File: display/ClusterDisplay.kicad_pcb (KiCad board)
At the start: 4 copper layers, 169.3 x 101.8 mm, 164 parts, among them J1 Verdin iMX95 Hexa 8GB WB IT, J10 RTC coin cell, J11 Molex KK-254 22-27-2041, rota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, J12 Samtec TSW-103-07-G-S A55 con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, J13 Samtec TSW-105-07-G-S USB_1 O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, J14 JST XH B5B-XH-A balanced line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, J15 JST XH B3B-XH-A electret micr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, J16 MFi coprocessor access I2C_1 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, J17 GCT USB4105-GF-A USB-C 2.0 ho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, J2 Phoenix MKDS 1,5/3-5,08 power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, J3 Molex KK-254 22-27-2031 priva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, J4 TST040HDBC-42 panel, J8 Samtec TSW-108-07-G-S JTAG (b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, J9 Samtec TSW-104-07-G-S buttons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, Q1 PMV55ENEA (AEC-Q101, 60V/20V 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, Q2 PMV55ENEA (AEC-Q101, 60V/20V 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, Q3 PMV55ENEA ignition wake pulld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, U1 LM74930-Q1, U10 TLV767-Q1 (3.3 V audio AVDD), U11 TPS2557-Q1, U12 TPD4E05U06-Q1 line-out ESD, U13 TPD4E05U06-Q1 mic ESD, U14 TPD4E05U06-Q1 USB ESD, U2 LM61460-Q1, U3 TLV767-Q1, U4 TCAN1044V-Q1, U6 TPS65131-Q1, U7 TPS61165-Q1, U8 TPS22918-Q1 (AEC-Q100 G2) dia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, U9 TAC5112-Q1

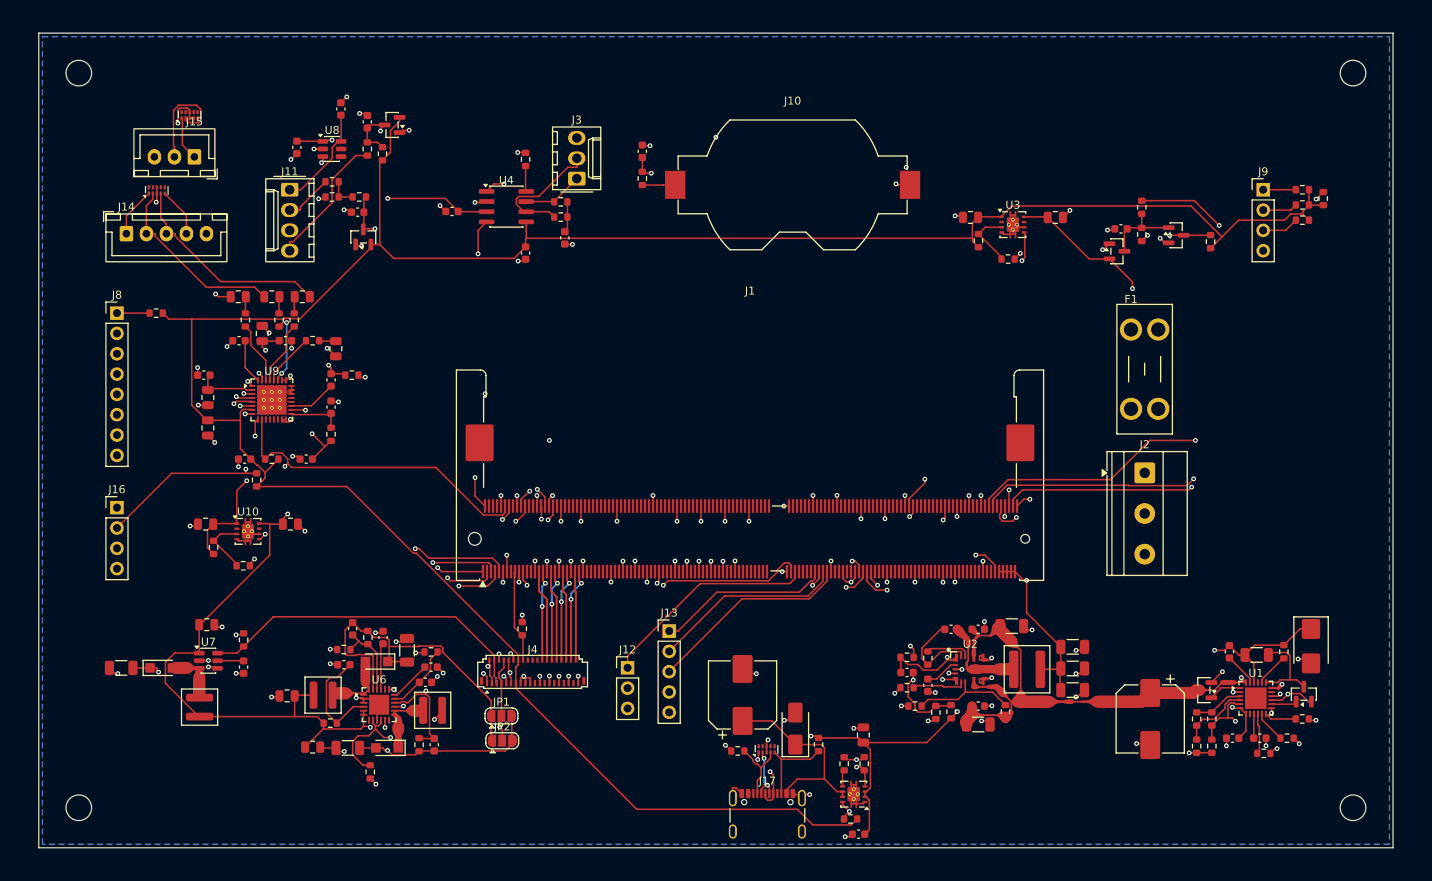
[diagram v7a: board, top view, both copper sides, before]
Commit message: Electrical review, part 2: +3V3 rail clamp on gauges, display battery path and TVS footprint, harness wording, new display parts reviewed
gauges/: D33 (onsemi SZMMSZ3V6T1G 3.6 V zener) clamps +3V3 when a sender wire is shorted to battery with the car off (G-08); BOM and connector values follow docs/harness.md (J7 DTM06-6S with a sealed cavity, J8 an in-dash KK 254 cable, 20/22 AWG). display/: D1 footprint D_SMB -> D_SMC to match the SMCJ33A in the BOM (D-01); VBAT_IN, VBAT_F, SENSE_OUT and COMMON added to TRUNK_NETS (D-02). review/expected.py covers the TAC5112-Q1, TPS2557-Q1, TPD4E05U06-Q1 and the second TLV767-Q1. Both boards regenerated and routed: real kicad-cli DRC 0 unconnected, only accepted categories; fab packages rebuilt.

Co-Authored-By: Claude Opus 5.5 <noreply@anthropic.com>
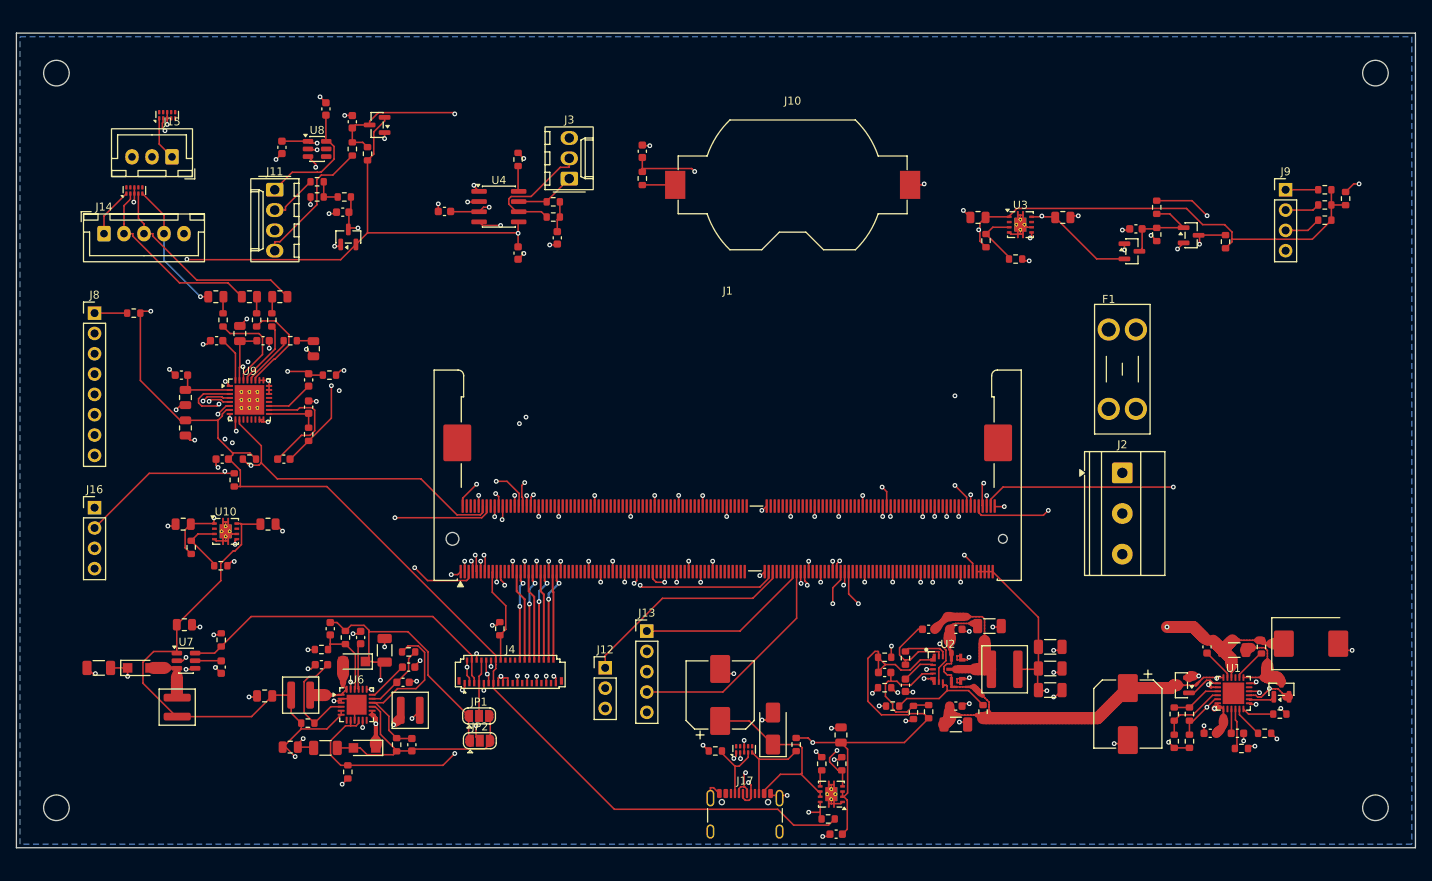
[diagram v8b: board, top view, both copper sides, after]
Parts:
- D1: footprint Diode_SMD:D_SMB -> Diode_SMD:D_SMC
- moved R4 2.87 mm to (275.7, 187.0)
- moved C1 2.87 mm to (261.5, 182.7)
- moved C3 2.87 mm to (271.4, 174.3)
- moved C4 2.87 mm to (275.2, 185.1)
- moved Q1 2.87 mm to (268.2, 179.1)
- moved Q2 2.87 mm to (280.7, 179.6)
- moved R15 2.87 mm to (280.5, 182.7)
- moved R2 2.87 mm to (278.2, 174.3)
- moved R3 2.87 mm to (278.6, 185.1)
- moved R5 2.87 mm to (269.2, 182.7)
- moved R6 2.87 mm to (269.2, 186.1)
- moved U1 2.87 mm to (274.7, 180.1)
- moved C2 2.87 mm to (271.8, 185.1)
- moved R1 2.87 mm to (274.8, 174.7)
- moved R7 2.87 mm to (267.3, 182.7)
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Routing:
- net +5V: track 393.3 -> 465.1 mm, vias 11 -> 8
- net JTAG_TMS: track 65.6 -> 99.1 mm
- net DIAL_CLICK: track 107.8 -> 93.2 mm, vias 3 -> 2
- net VBAT_F: track 77.9 -> 89.2 mm
- net GND: track 217.6 -> 207.6 mm, vias 144 -> 145
- net RT_5V: track 6.72 -> 16.2 mm, vias 0 -> 2
- net PWR_EN_MOCI: track 133.7 -> 143.0 mm
- net JTAG_VREF: track 75.4 -> 66.2 mm, vias 1 -> 2
- net PANEL_BIAS_EN: track 40.7 -> 49.5 mm
- net PWR_BTN: track 72.2 -> 65.1 mm
- net MIC_N: track 51.6 -> 44.7 mm, vias 1 -> 2
- net RESET_MOCI: track 67.5 -> 73.9 mm
- net +1V8: track 312.1 -> 318.5 mm, vias 0 -> 4
- net SW_5V: track 11.6 -> 17.7 mm
- net I2S_FSYNC: track 49.2 -> 55.2 mm, vias 2 -> 3
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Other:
- board size 169.3 x 101.8 mm -> 174.9 x 101.8 mm
